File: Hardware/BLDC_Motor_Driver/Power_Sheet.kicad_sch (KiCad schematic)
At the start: 0 parts

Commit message: Add buck converter IC 36V input to 3.3V
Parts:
- added C1, C3, C4, C7, C8: 100nF, Capacitor_SMD:C_0603_1608Metric, symbol Device:C
- added C10, C5, C6, C9: 47uF, Capacitor_SMD:C_1206_3216Metric, symbol Device:C
- added C2: 33pF, Capacitor_SMD:C_0603_1608Metric, symbol Device:C
- added L1: 2.2uH, Inductor_SMD:L_TechFuse_SL0420, symbol Device:L
- added R1, R4: 0R, Resistor_SMD:R_0603_1608Metric, symbol Device:R
- added R2, R5, R6, R7: 100K, Resistor_SMD:R_0603_1608Metric, symbol Device:R
- added R3: 31.6K, Resistor_SMD:R_0603_1608Metric, symbol Device:R
- added R8: 1K, Resistor_SMD:R_0603_1608Metric, symbol Device:R
- added U1: LMR51440SDRRR, BLDC_Motor_Driver_Components_Footprint:CONV_LMR51440SDRRR, symbol LMR51440SDRRR:LMR51440SDRRR
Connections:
- new net: R1.1, U1.6 (RT)
- new net: C1.2, L1.1, U1.1 (SW), U1.2 (SW), U1.3 (SW)
- new net: C1.1, U1.4 (BOOT)
- new net: C2.2, R2.2, R3.1, U1.7 (FB)
- new net: C2.1, R8.2
- new net +18V: R5.2, R6.1, R7.1
- new net +3.3V: C3.2, C4.2, C5.2, C6.2, L1.2, R2.1, R8.1
- new net +36V: R5.1
- new net AGND: R1.2, R3.2, R4.2, R6.2, U1.8 (AGND)
- new net GND: C10.1, C3.1, C4.1, C5.1, C6.1, C7.1, C8.1, C9.1, U1.13 (PGND)
- new net PG: R4.1, R7.2, U1.5 (PG)
- new net Vin: C10.2, C7.2, C8.2, C9.2, U1.10 (VIN), U1.11 (VIN), U1.12 (VIN), U1.9 (EN)
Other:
- note added: "For 1MHz Switching Frequency RT = 13.3K ohm or RT shorten to ground for 13.3K ohm we can replce resistor with MP: FRC0603F1332TS For 440KHz switching Frequency RT pulled up to VCC but max 5V"
- note added: "Open-drain power-good monitor output that asserts low if the FB voltage is not within the specified window thresholds. A 10kΩ to 100kΩ pull up resistor to a suitable voltage is required.If not used, PG can be left open or connected to GND."
- note added: "Rfbb"
- note added: "Rfbt"

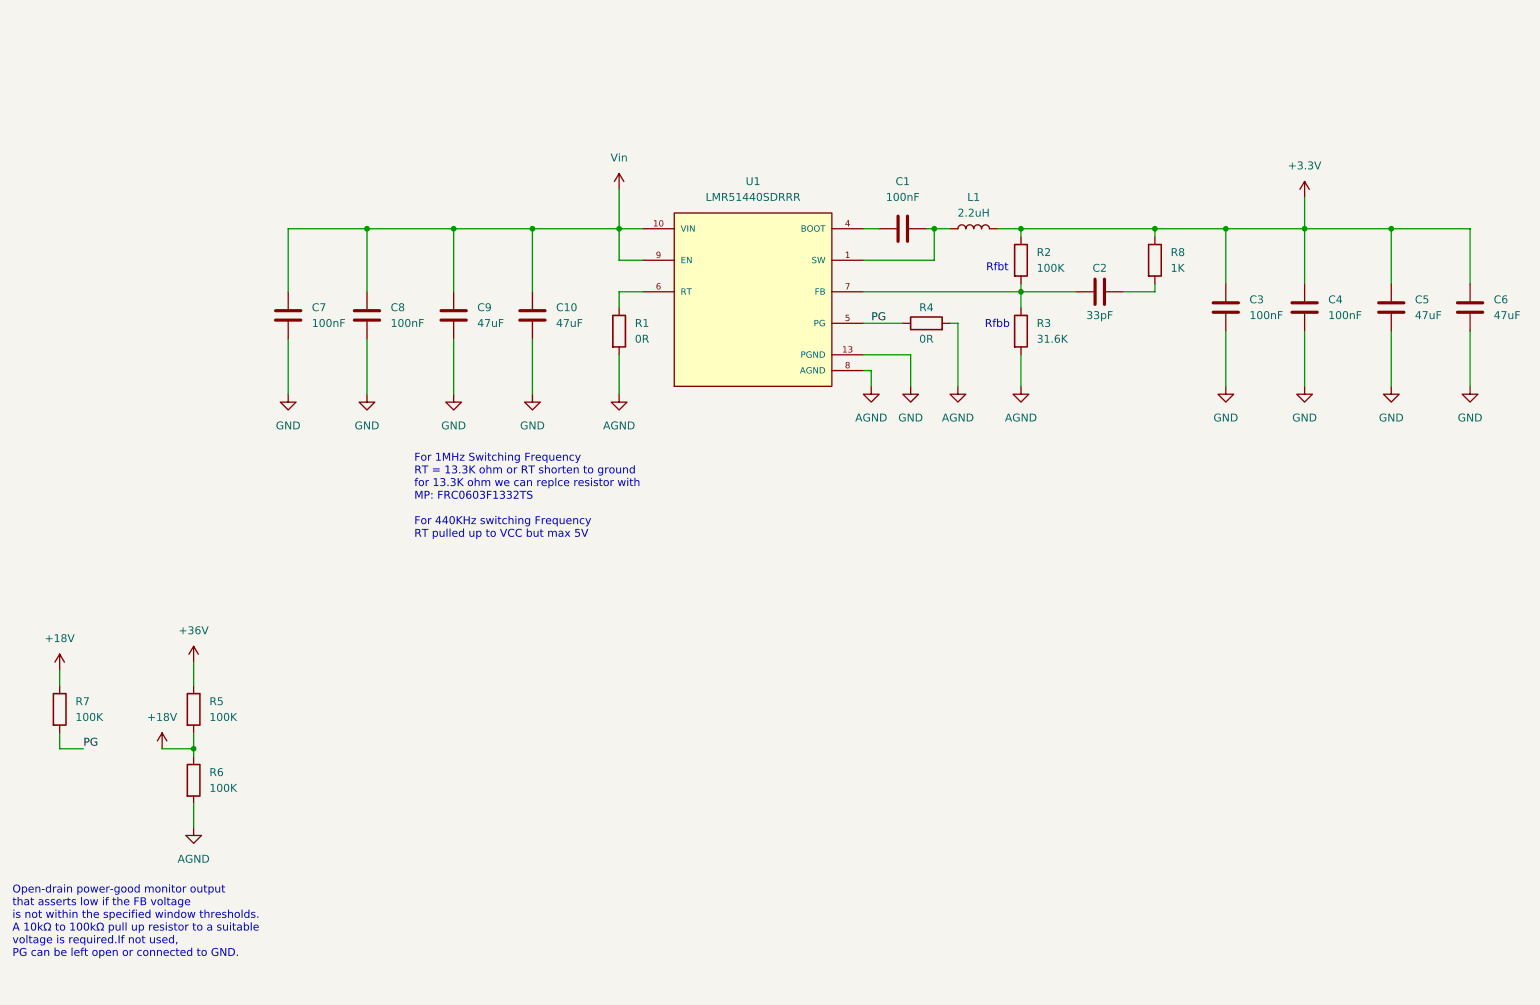
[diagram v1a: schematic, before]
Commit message: Add Selection of CAN IC and arrange the sheet of buck converter
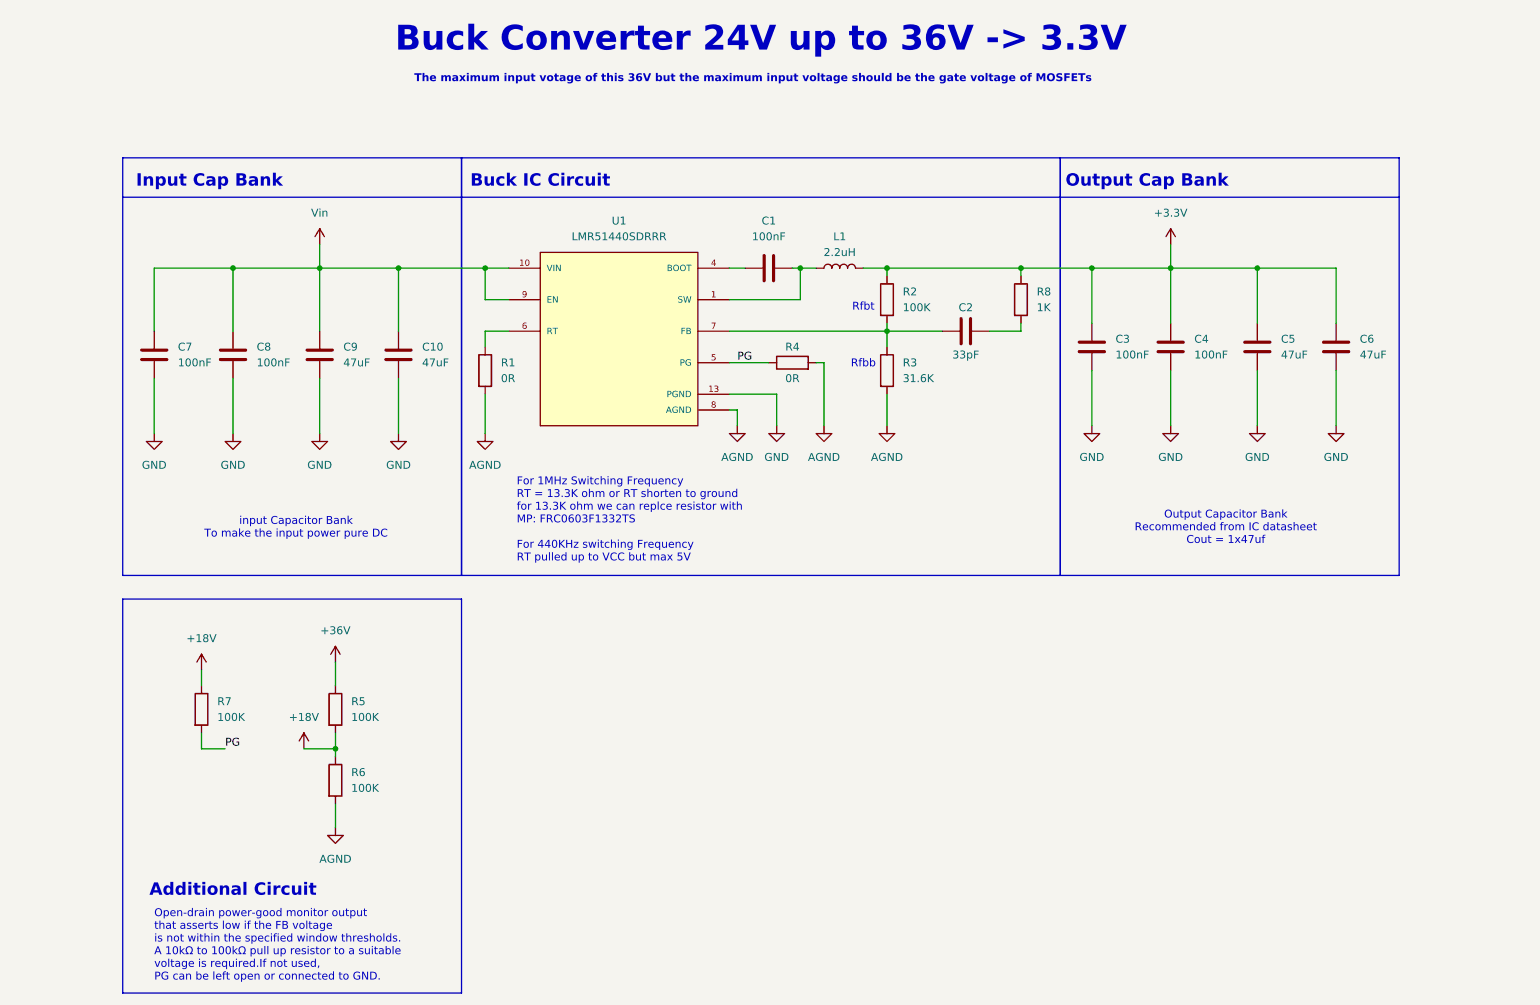
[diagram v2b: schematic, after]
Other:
- note added: "Additional Circuit"
- note added: "Buck Converter 24V up to 36V -> 3.3V"
- note added: "Buck IC Circuit"
- note added: "Input Cap Bank"
- note added: "Output Cap Bank"
- note added: "Output Capacitor Bank Recommended from IC datasheet Cout = 1x47uf"
- note added: "The maximum input votage of this 36V but the maximum input voltage should be the gate voltage of MOSFETs"
- note added: "input Capacitor Bank To make the input power pure DC"
- title: (none) -> ${Project_Name}
- moved on the sheet: C1, C10, C2, C3, C4, C5, C6, C7, C8, C9, L1, R1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
